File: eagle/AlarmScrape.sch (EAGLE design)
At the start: 24 parts, among them IC1 LM339D, Q2 POW-EBAY, SW1 TACTILE-2, T1 2222, X1 POW, X2 Z12, X3 Z34

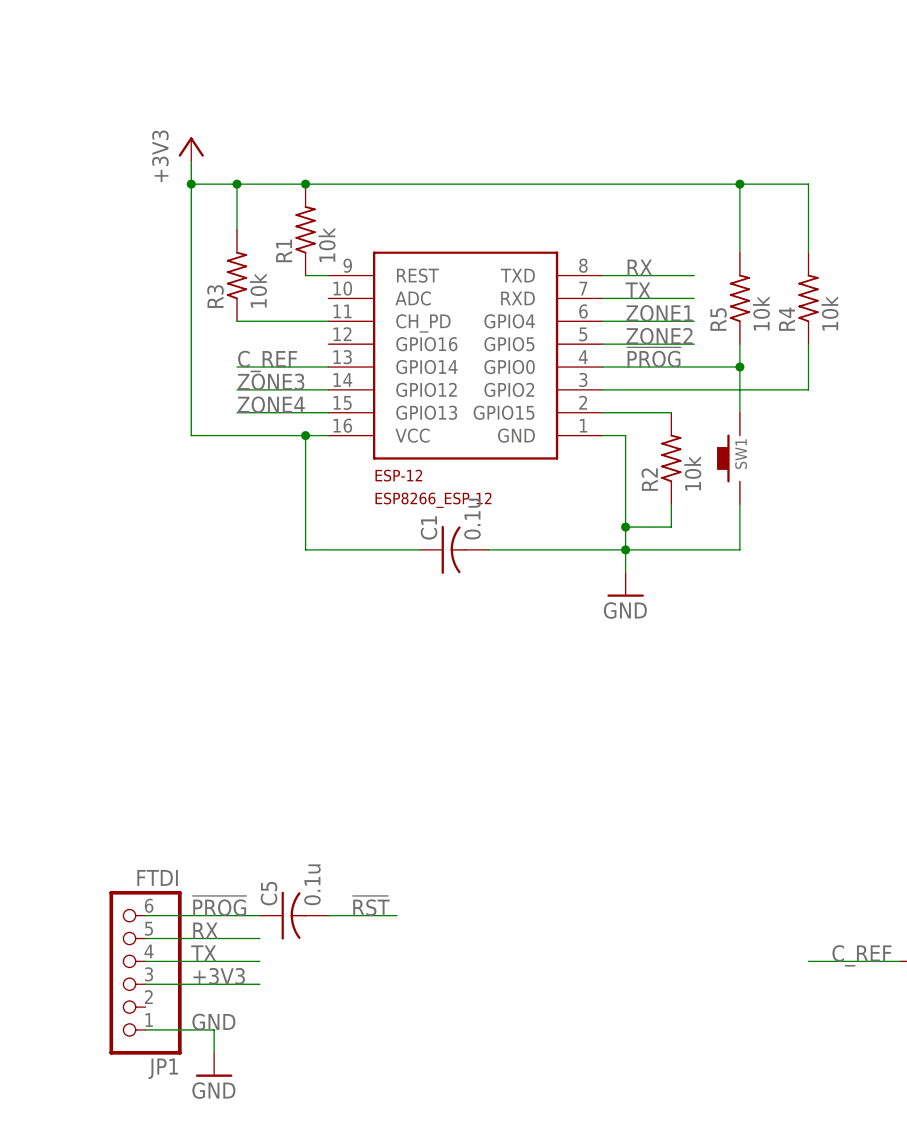
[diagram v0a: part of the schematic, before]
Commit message: PCB rev 2
-- Added LED
-- Removed !RESET pullup
-- Disconnected RTS from GP0 and !RESET
-- FTDI VCC now connected to VIN instead of 3.3V
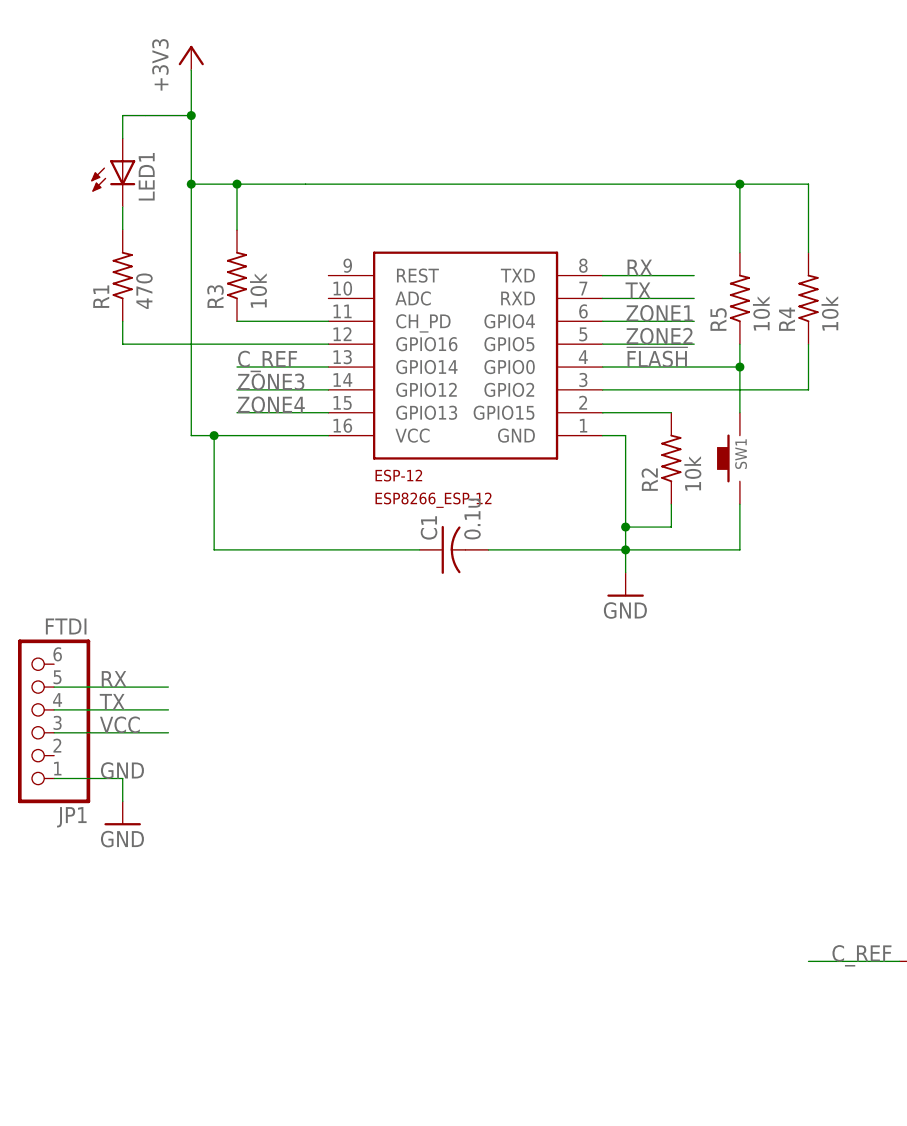
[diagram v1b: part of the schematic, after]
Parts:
- removed C5: 0.1u, resistor:C-USC0805
- added LED1: (no value), led:LEDCHIPLED_0805
- R1: value 10k -> 470
- SW1: value TACTILE-2 -> FLASH
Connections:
- removed net !PROG: C5.1, ESP-12.GPIO0, JP1.6, R5.1, SW1.P1
- removed net !RST: C5.2, ESP-12.REST, R1.1
- new net !FLASH: ESP-12.GPIO0, R5.1, SW1.P1
- new net N$1: ESP-12.GPIO16, R1.1
- new net N$4: LED1.C, R1.2
- net +3V3: now also LED1.A; no longer JP1.3, R1.2
- net VCC: now also JP1.3
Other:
- moved on the sheet: JP1, R1
